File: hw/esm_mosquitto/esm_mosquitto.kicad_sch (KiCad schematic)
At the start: 16 parts

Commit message: Компоновка завершена
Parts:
- added D1, D2, D3: (no value), symbol Device:LED
- added R10, R8, R9: (no value), symbol Device:R
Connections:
- net +5V: now also J1.1 (Pin_1)
- net GND: now also J1.2 (Pin_2), D1.1 (K), D2.1 (K), D3.1 (K)
- net A0: now reaches J1.4 (Pin_4)
- net A0: now also A1.19 (A0)
- net at A1.5 (D2): now also R8.2
- net at A1.6 (D3): now also R9.2
- net at A1.7 (D4): now also R10.2
- new net: D3.2 (A), R10.1
- new net: D2.2 (A), R9.1
- new net: D1.2 (A), R8.1
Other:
- moved on the sheet: J1, U1, U3

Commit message: Собрано устройство на паечной макетной плате. Исправлены ошибки при монтаже, проверены напряжения питания. Изменена схема формирования напряжения 3.3 В, переназначены выводы для светодиодов и датчика DHT 22
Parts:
- removed C1: (no value), symbol Device:C
- removed C2: (no value), symbol Device:C_Polarized
- removed R6, R7: (no value), symbol Device:R
- removed U4: (no value), symbol Regulator_Linear:LM317_TO-220
- added C1: 220u, Capacitor_THT:CP_Radial_D5.0mm_P2.50mm, symbol Device:C_Polarized
- added C3, C4: (no value), symbol pspice:C
- added U5: (no value), symbol Regulator_Linear:AMS1117-3.3
- D2: value (none) -> LED_Y_soil; footprint (none) -> LED_THT:LED_D5.0mm_Clear
- D3: value (none) -> LED_R_mqtt; footprint (none) -> LED_THT:LED_D5.0mm_Clear
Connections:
- net +3V3: now also C4.1, U5.2 (VO)
- net +5V: now also J2.1, C1.1, C3.1, U5.3 (VI)
- net DHT_OUT: now also A1.14 (D11); no longer A1.9 (D6)
- net GND: now also C1.2, C3.2, C4.2, U5.1 (GND)
- net at R10.2: now also A1.11 (D8); no longer A1.7 (D4)
- net at R8.2: now also A1.9 (D6); no longer A1.5 (D2)
- net at R9.2: now also A1.10 (D7); no longer A1.6 (D3)
- net VIN: no longer names the net of A1.30 (VIN)
- net VIN: no longer J2.1
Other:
- moved on the sheet: J2

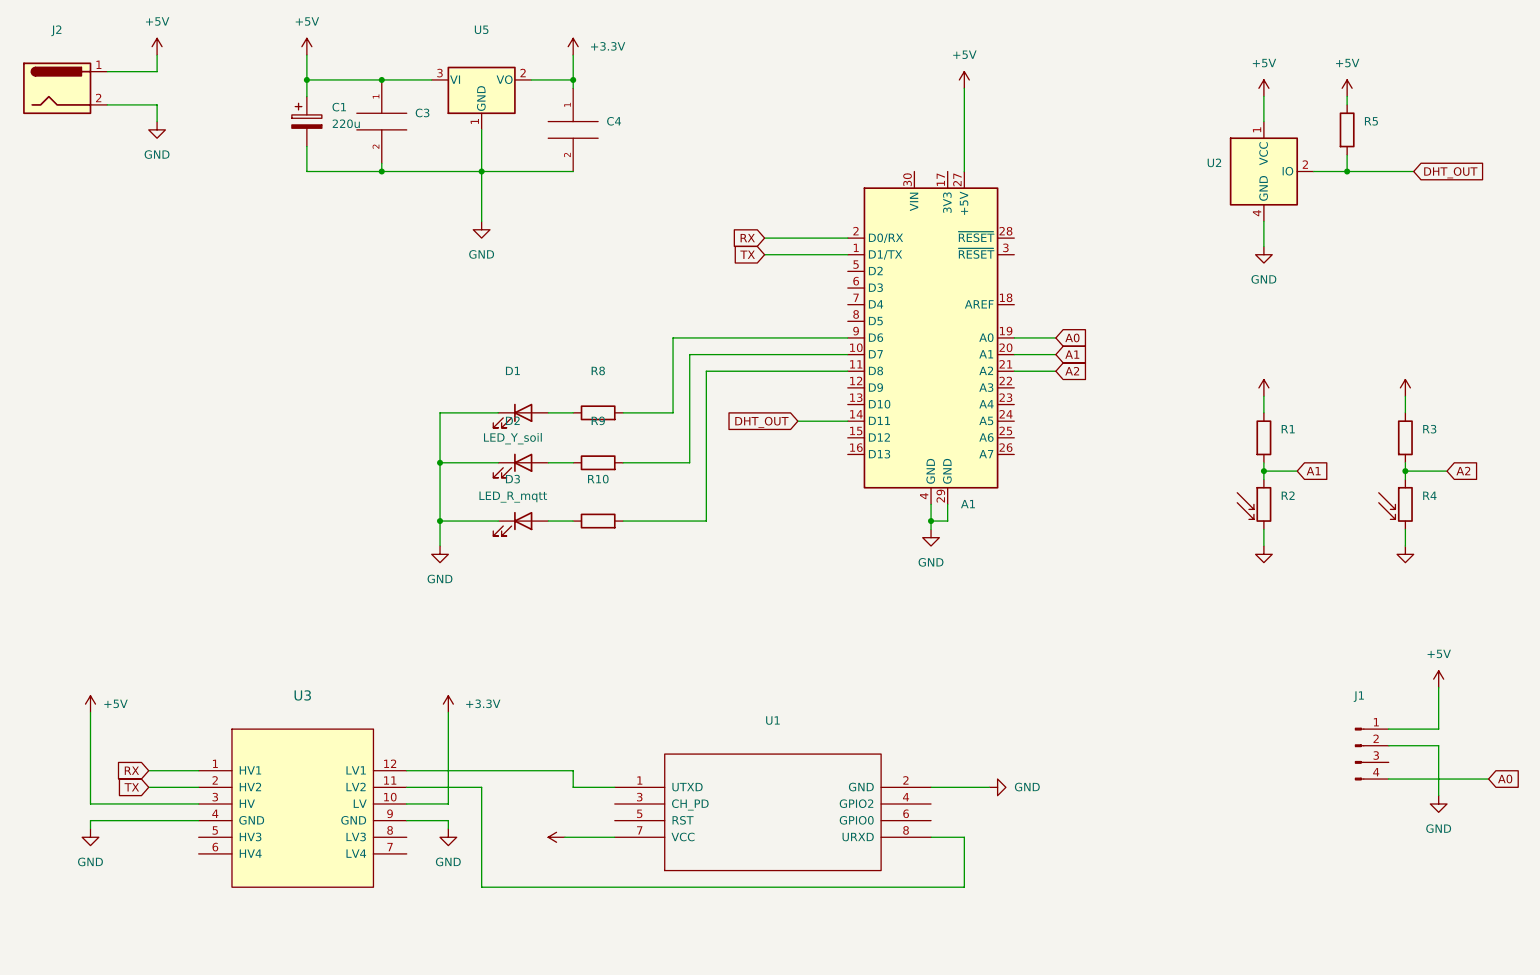
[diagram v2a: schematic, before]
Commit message: - Исправлена ошибка в подключении ESP 01: вывод EN подтянут к питанию - Допаяны последние провода - Устройство собрано в корпус
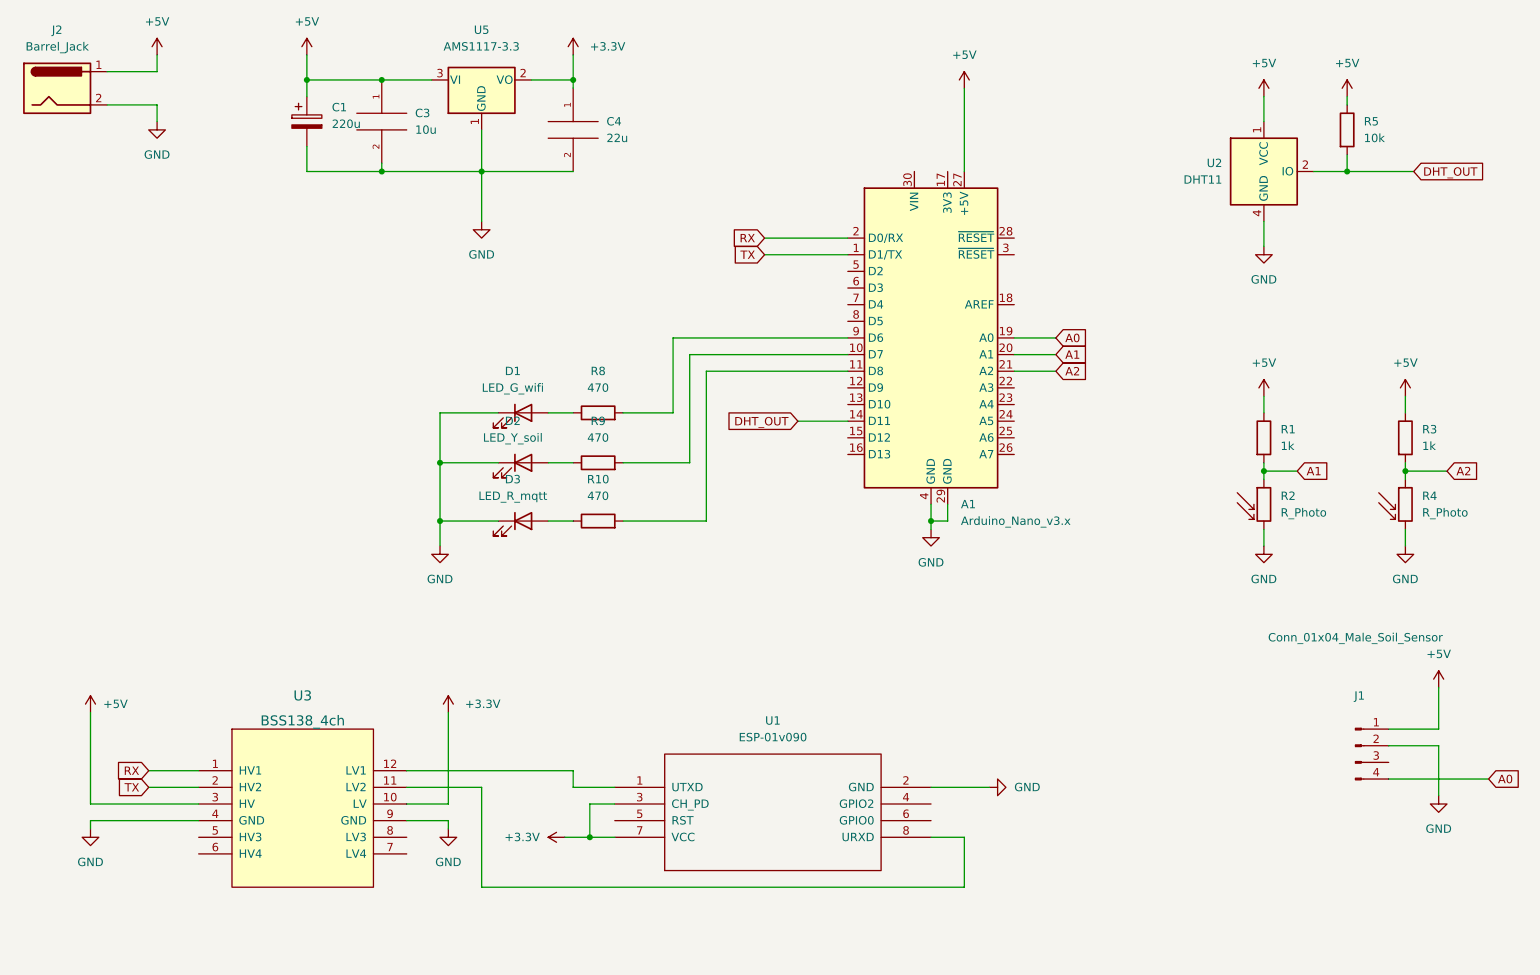
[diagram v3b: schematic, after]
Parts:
- A1: value (none) -> Arduino_Nano_v3.x; footprint (none) -> Module:Arduino_Nano
- C3: value (none) -> 10u; footprint (none) -> Capacitor_SMD:C_0805_2012Metric
- C4: value (none) -> 22u; footprint (none) -> Capacitor_SMD:C_0805_2012Metric
- D1: value (none) -> LED_G_wifi; footprint (none) -> LED_THT:LED_D5.0mm_Clear
- J1: value (none) -> Conn_01x04_Male_Soil_Sensor; footprint (none) -> Connector_PinHeader_2.54mm:PinHeader_1x04_P2.54mm_Vertical
- J2: value (none) -> Barrel_Jack; footprint (none) -> TerminalBlock:TerminalBlock_Altech_AK300-2_P5.00mm
- R1, R3: value (none) -> 1k; footprint (none) -> Resistor_THT:R_Axial_DIN0207_L6.3mm_D2.5mm_P7.62mm_Horizontal
- R10, R8, R9: value (none) -> 470; footprint (none) -> Resistor_THT:R_Axial_DIN0207_L6.3mm_D2.5mm_P7.62mm_Horizontal
- R2, R4: value (none) -> R_Photo; footprint (none) -> Connector_PinHeader_2.54mm:PinHeader_1x02_P2.54mm_Vertical
- R5: value (none) -> 10k; footprint (none) -> Resistor_THT:R_Axial_DIN0207_L6.3mm_D2.5mm_P7.62mm_Horizontal
- U1: value (none) -> ESP-01v090; footprint (none) -> ESP-01:ESP-01
- U2: value (none) -> DHT11; footprint (none) -> Sensor:Aosong_DHT11_5.5x12.0_P2.54mm
- U3: value (none) -> BSS138_4ch; footprint (none) -> Logic_Level_Converter:BSS138
- U5: value (none) -> AMS1117-3.3; footprint (none) -> Package_TO_SOT_SMD:SOT-223-3_TabPin2
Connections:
- net +3V3: now also U1.3 (CH_PD)

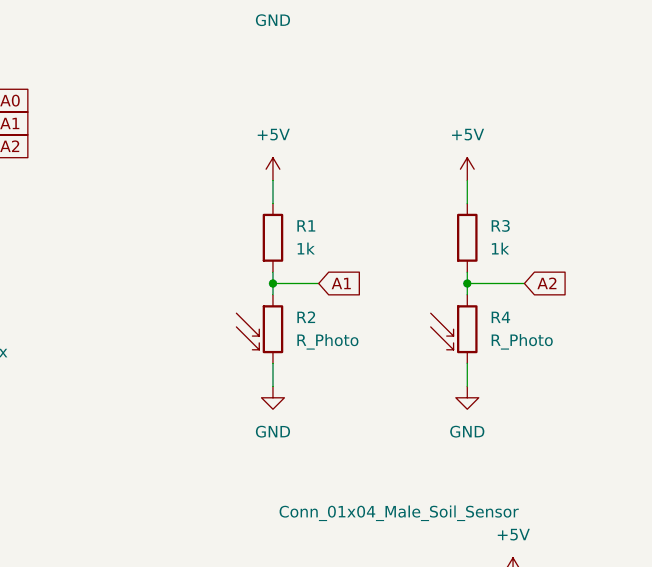
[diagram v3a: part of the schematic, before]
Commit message: - Исправлено подключение фоторезисторов: фоторезистор и резистор 1к поменяны местами - Допаян длинный провод для вилки датчика влажности почвы - Устройство проверено, работает как ожидается
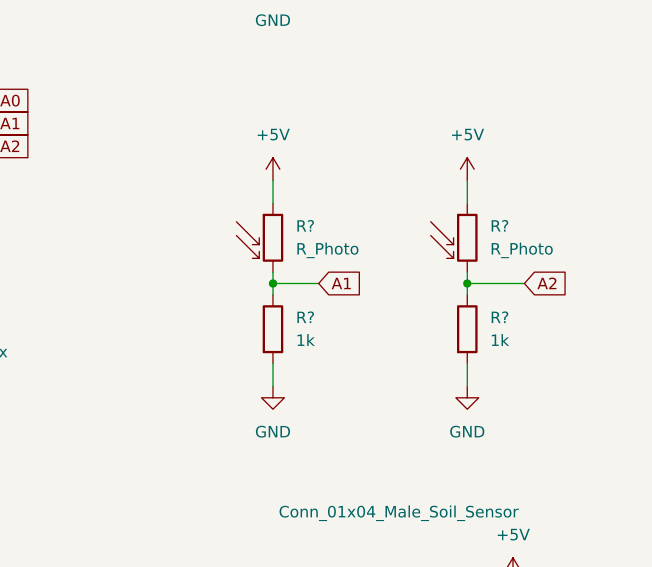
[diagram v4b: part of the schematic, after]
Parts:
- removed R1, R3: 1k, Resistor_THT:R_Axial_DIN0207_L6.3mm_D2.5mm_P7.62mm_Horizontal, symbol Device:R
- removed R2, R4: R_Photo, Connector_PinHeader_2.54mm:PinHeader_1x02_P2.54mm_Vertical, symbol Device:R_Photo
- added R? (x2): 1k, Resistor_THT:R_Axial_DIN0207_L6.3mm_D2.5mm_P7.62mm_Horizontal, symbol Device:R
- added R? (x2): R_Photo, Connector_PinHeader_2.54mm:PinHeader_1x02_P2.54mm_Vertical, symbol Device:R_Photo
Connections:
- net +5V: now also R?.1, R?.1
- net A1: now also R?.1, R?.2
- net A2: now also R?.1, R?.2
- net GND: now also R?.2, R?.2
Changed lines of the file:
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@@
+    (pin "2")
+  )
+  (symbol (lib_id "Device:R") (at 208.28 93.98 0) (unit 1)
+    (in_bom yes) (on_board yes) (fields_autoplaced)
+    (property "Reference" "R?" (id 0) (at 210.82 92.7099 0)
+      (effects (font (size 1.27 1.27)) (justify left))
+    )
+    (property "Value" "1k" (id 1) (at 210.82 95.2499 0)
+      (effects (font (size 1.27 1.27)) (justify left))
+    )
+    (property "Footprint" "Resistor_THT:R_Axial_DIN0207_L6.3mm_D2.5mm_P7.62mm_Horizontal" (id 2) (at 206.502 93.98 90)
+      (effects (font (size 1.27 1.27)) hide)
+    )
+    (property "Datasheet" "~" (id 3) (at 208.28 93.98 0)
+      (effects (font (size 1.27 1.27)) hide)
+    )
+    (pin "1")
     (pin "2")
   )
@@
     (pin "1")
   )
-  (symbol (lib_id "Device:R") (at 229.87 83.82 0) (unit 1)
-    (in_bom yes) (on_board yes) (fields_autoplaced)
-    (property "Reference" "R3" (id 0) (at 232.41 82.5499 0)
-      (effects (font (size 1.27 1.27)) (justify left))
-    )
-    (property "Value" "1k" (id 1) (at 232.41 85.0899 0)
-      (effects (font (size 1.27 1.27)) (justify left))
-    )
-    (property "Footprint" "Resistor_THT:R_Axial_DIN0207_L6.3mm_D2.5mm_P7.62mm_Horizontal" (id 2) (at 228.092 83.82 90)
-      (effects (font (size 1.27 1.27)) hide)
-    )
-    (property "Datasheet" "~" (id 3) (at 229.87 83.82 0)
-      (effects (font (size 1.27 1.27)) hide)
-    )
-    (pin "1")
-    (pin "2")
-  )
   (symbol (lib_id "Device:R") (at 106.68 96.52 90) (unit 1)
     (in_bom yes) (on_board yes) (fields_autoplaced)
@@
     )
     (pin "1")
+  )
+  (symbol (lib_id "Device:R_Photo") (at 208.28 83.82 0) (unit 1)
+    (in_bom yes) (on_board yes) (fields_autoplaced)
+    (property "Reference" "R?" (id 0) (at 210.82 82.5499 0)
+      (effects (font (size 1.27 1.27)) (justify left))
+    )
+    (property "Value" "R_Photo" (id 1) (at 210.82 85.0899 0)
+      (effects (font (size 1.27 1.27)) (justify left))
+    )
+    (property "Footprint" "Connector_PinHeader_2.54mm:PinHeader_1x02_P2.54mm_Vertical" (id 2) (at 209.55 90.17 90)
+      (effects (font (size 1.27 1.27)) (justify left) hide)
+    )
+    (property "Datasheet" "~" (id 3) (at 208.28 85.09 0)
+      (effects (font (size 1.27 1.27)) hide)
+    )
+    (pin "1")
+    (pin "2")
   )
   (symbol (lib_id "power:GND") (at 157.48 97.79 0) (unit 1)
@@
     )
     (property "Datasheet" "~" (id 3) (at 62.23 35.56 0)
+      (effects (font (size 1.27 1.27)) hide)
+    )
+    (pin "1")
+    (pin "2")
+  )
+  (symbol (lib_id "Device:R_Photo") (at 229.87 83.82 0) (unit 1)
+    (in_bom yes) (on_board yes) (fields_autoplaced)
+    (property "Reference" "R?" (id 0) (at 232.41 82.5499 0)
+      (effects (font (size 1.27 1.27)) (justify left))
+    )
+    (property "Value" "R_Photo" (id 1) (at 232.41 85.0899 0)
+      (effects (font (size 1.27 1.27)) (justify left))
+    )
+    (property "Footprint" "Connector_PinHeader_2.54mm:PinHeader_1x02_P2.54mm_Vertical" (id 2) (at 231.14 90.17 90)
+      (effects (font (size 1.27 1.27)) (justify left) hide)
+    )
+    (property "Datasheet" "~" (id 3) (at 229.87 85.09 0)
       (effects (font (size 1.27 1.27)) hide)
     )
@@
     (pin "9")
   )
-  (symbol (lib_id "Device:R") (at 208.28 83.82 0) (unit 1)
-    (in_bom yes) (on_board yes) (fields_autoplaced)
-    (property "Reference" "R1" (id 0) (at 210.82 82.5499 0)
-      (effects (font (size 1.27 1.27)) (justify left))
-    )
-    (property "Value" "1k" (id 1) (at 210.82 85.0899 0)
-      (effects (font (size 1.27 1.27)) (justify left))
-    )
-    (property "Footprint" "Resistor_THT:R_Axial_DIN0207_L6.3mm_D2.5mm_P7.62mm_Horizontal" (id 2) (at 206.502 83.82 90)
-      (effects (font (size 1.27 1.27)) hide)
-    )
-    (property "Datasheet" "~" (id 3) (at 208.28 83.82 0)
-      (effects (font (size 1.27 1.27)) hide)
-    )
-    (pin "1")
-    (pin "2")
-  )
   (symbol (lib_id "ESP-01:ESP-01v090") (at 133.35 140.97 0) (unit 1)
     (in_bom yes) (on_board yes) (fields_autoplaced)
@@
     (pin "2")
   )
+  (symbol (lib_id "Device:R") (at 229.87 93.98 0) (unit 1)
+    (in_bom yes) (on_board yes) (fields_autoplaced)
+    (property "Reference" "R?" (id 0) (at 232.41 92.7099 0)
+      (effects (font (size 1.27 1.27)) (justify left))
+    )
+    (property "Value" "1k" (id 1) (at 232.41 95.2499 0)
+      (effects (font (size 1.27 1.27)) (justify left))
+    )
+    (property "Footprint" "Resistor_THT:R_Axial_DIN0207_L6.3mm_D2.5mm_P7.62mm_Horizontal" (id 2) (at 228.092 93.98 90)
+      (effects (font (size 1.27 1.27)) hide)
+    )
+    (property "Datasheet" "~" (id 3) (at 229.87 93.98 0)
+      (effects (font (size 1.27 1.27)) hide)
+    )
+    (pin "1")
+    (pin "2")
+  )
   (symbol (lib_id "power:GND") (at 234.95 138.43 0) (unit 1)
     (in_bom yes) (on_board yes) (fields_autoplaced)
@@
     (pin "3")
     (pin "4")
-  )
-  (symbol (lib_id "Device:R_Photo") (at 229.87 93.98 0) (unit 1)
-    (in_bom yes) (on_board yes) (fields_autoplaced)
-    (property "Reference" "R4" (id 0) (at 232.41 92.7099 0)
-      (effects (font (size 1.27 1.27)) (justify left))
-    )
-    (property "Value" "R_Photo" (id 1) (at 232.41 95.2499 0)
-      (effects (font (size 1.27 1.27)) (justify left))
-    )
-    (property "Footprint" "Connector_PinHeader_2.54mm:PinHeader_1x02_P2.54mm_Vertical" (id 2) (at 231.14 100.33 90)
-      (effects (font (size 1.27 1.27)) (justify left) hide)
-    )
-    (property "Datasheet" "~" (id 3) (at 229.87 95.25 0)
-      (effects (font (size 1.27 1.27)) hide)
-    )
-    (pin "1")
-    (pin "2")
-  )
-  (symbol (lib_id "Device:R_Photo") (at 208.28 93.98 0) (unit 1)
-    (in_bom yes) (on_board yes) (fields_autoplaced)
-    (property "Reference" "R2" (id 0) (at 210.82 92.7099 0)
-      (effects (font (size 1.27 1.27)) (justify left))
-    )
-    (property "Value" "R_Photo" (id 1) (at 210.82 95.2499 0)
-      (effects (font (size 1.27 1.27)) (justify left))
-    )
-    (property "Footprint" "Connector_PinHeader_2.54mm:PinHeader_1x02_P2.54mm_Vertical" (id 2) (at 209.55 100.33 90)
-      (effects (font (size 1.27 1.27)) (justify left) hide)
-    )
-    (property "Datasheet" "~" (id 3) (at 208.28 95.25 0)
-      (effects (font (size 1.27 1.27)) hide)
-    )
-    (pin "1")
-    (pin "2")
   )
   (symbol (lib_id "power:+5V") (at 162.56 30.48 0) (unit 1)
@@
       (reference "J2") (unit 1) (value "Barrel_Jack") (footprint "TerminalBlock:TerminalBlock_Altech_AK300-2_P5.00mm")
     )
-    (path "/89aed4c2-7165-41f8-9b65-bee5cec34e33"
-      (reference "R1") (unit 1) (value "1k") (footprint "Resistor_THT:R_Axial_DIN0207_L6.3mm_D2.5mm_P7.62mm_Horizontal")
-    )
-    (path "/c2d71c1d-5123-413a-bc27-a657fa23d2d7"
-      (reference "R2") (unit 1) (value "R_Photo") (footprint "Connector_PinHeader_2.54mm:PinHeader_1x02_P2.54mm_Vertical")
-    )
-    (path "/4dc795bb-4b79-4995-9679-d61c9f829928"
-      (reference "R3") (unit 1) (value "1k") (footprint "Resistor_THT:R_Axial_DIN0207_L6.3mm_D2.5mm_P7.62mm_Horizontal")
-    )
-    (path "/c0d6207b-ac4b-4460-b3c0-c2c9825a91c2"
-      (reference "R4") (unit 1) (value "R_Photo") (footprint "Connector_PinHeader_2.54mm:PinHeader_1x02_P2.54mm_Vertical")
-    )
     (path "/9dcbe3b2-8052-429a-b956-ccd7c975e4f0"
       (reference "R5") (unit 1) (value "10k") (footprint "Resistor_THT:R_Axial_DIN0207_L6.3mm_D2.5mm_P7.62mm_Horizontal")
@@
       (reference "R10") (unit 1) (value "470") (footprint "Resistor_THT:R_Axial_DIN0207_L6.3mm_D2.5mm_P7.62mm_Horizontal")
     )
+    (path "/1e3fd3d5-91a2-4915-bf3d-e5e3d46d180b"
+      (reference "R?") (unit 1) (value "1k") (footprint "Resistor_THT:R_Axial_DIN0207_L6.3mm_D2.5mm_P7.62mm_Horizontal")
+    )
+    (path "/66a63530-21d0-4c46-9871-3b13e24c24f3"
+      (reference "R?") (unit 1) (value "R_Photo") (footprint "Connector_PinHeader_2.54mm:PinHeader_1x02_P2.54mm_Vertical")
+    )
+    (path "/7db2a4b9-f872-48cc-a2a7-1f09e20dda1e"
+      (reference "R?") (unit 1) (value "R_Photo") (footprint "Connector_PinHeader_2.54mm:PinHeader_1x02_P2.54mm_Vertical")
+    )
+    (path "/a681347c-2da8-48f2-88a6-f192a29fe2c6"
+      (reference "R?") (unit 1) (value "1k") (footprint "Resistor_THT:R_Axial_DIN0207_L6.3mm_D2.5mm_P7.62mm_Horizontal")
+    )
     (path "/9826698f-7603-4370-b8fe-754eff05d0c9"
